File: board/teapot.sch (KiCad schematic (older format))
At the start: 42 parts, among them P1 BATT, P2 SMA, Q1 TEPT4400, U1 TPS79333DBVR, U2 TLV61225, U3 microusb-b, U4 RFM69W, U5 STM32L052K8, U6 HTU21D, U7 MS5637, U8 SWD, Y1 32.768k

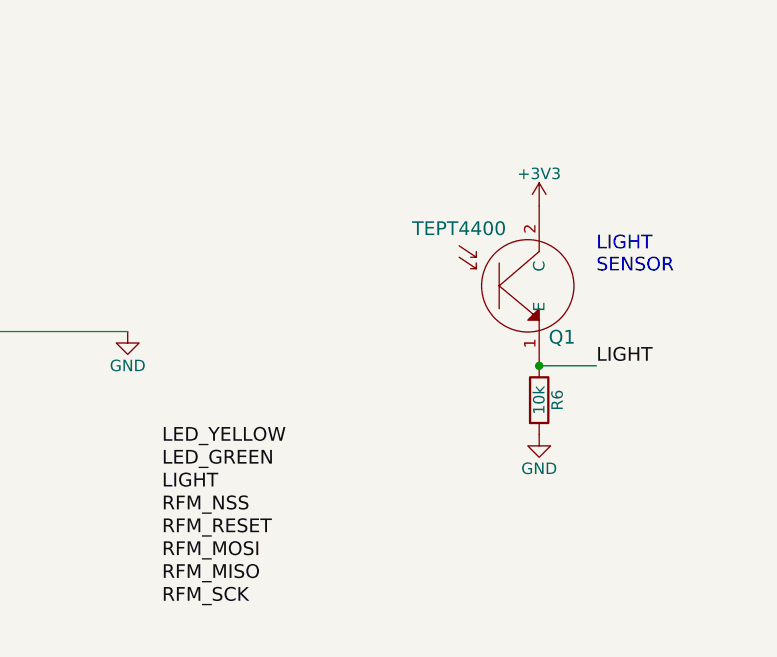
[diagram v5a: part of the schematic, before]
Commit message: Power consumption calculations
Resolves #5, resolves #2
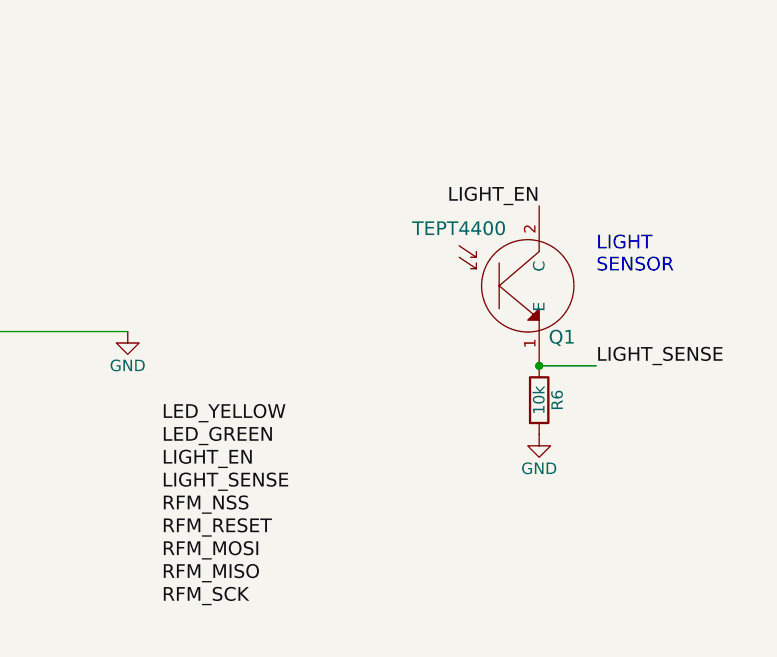
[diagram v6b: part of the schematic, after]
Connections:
- net +3V3: no longer Q1.2 (C)
- net LIGHT renamed LIGHT_SENSE
- new net LIGHT_EN: Q1.2 (C)
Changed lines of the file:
@@
-$EndComp
-$Comp
-L +3V3 #PWR013
-U 1 1 56709B94
-P 10200 3300
-F 0 "#PWR013" H 10200 3150 50  0001 C CNN
-F 1 "+3V3" H 10200 3440 50  0000 C CNN
-F 2 "" H 10200 3300 50  0000 C CNN
-F 3 "" H 10200 3300 50  0000 C CNN
-	1    10200 3300
-	1    0    0    -1
 $EndComp
 $Comp
@@
 I2C_SCK
 Text Label 10450 4000 0    60   ~ 0
-LIGHT
+LIGHT_SENSE
 Text Label 8750 1000 2    60   ~ 0
 RFM_RESET
@@
 I2C_SDA
 Text Label 8550 4550 0    60   ~ 0
-LIGHT
+LIGHT_SENSE
 Text Label 8550 4750 0    60   ~ 0
 RFM_RESET
@@
 	1    0    0    -1
 $EndComp
+Text Label 8550 4250 0    60   ~ 0
+LED_YELLOW
 Text Label 8550 4350 0    60   ~ 0
-LED_YELLOW
-Text Label 8550 4450 0    60   ~ 0
 LED_GREEN
 Text Label 1400 2850 2    60   ~ 0
@@
 	10650 1800 10800 1800
 Connection ~ 10800 1800
+Text Label 8550 4450 0    60   ~ 0
+LIGHT_EN
+Text Label 10200 3300 2    60   ~ 0
+LIGHT_EN
 $EndSCHEMATC

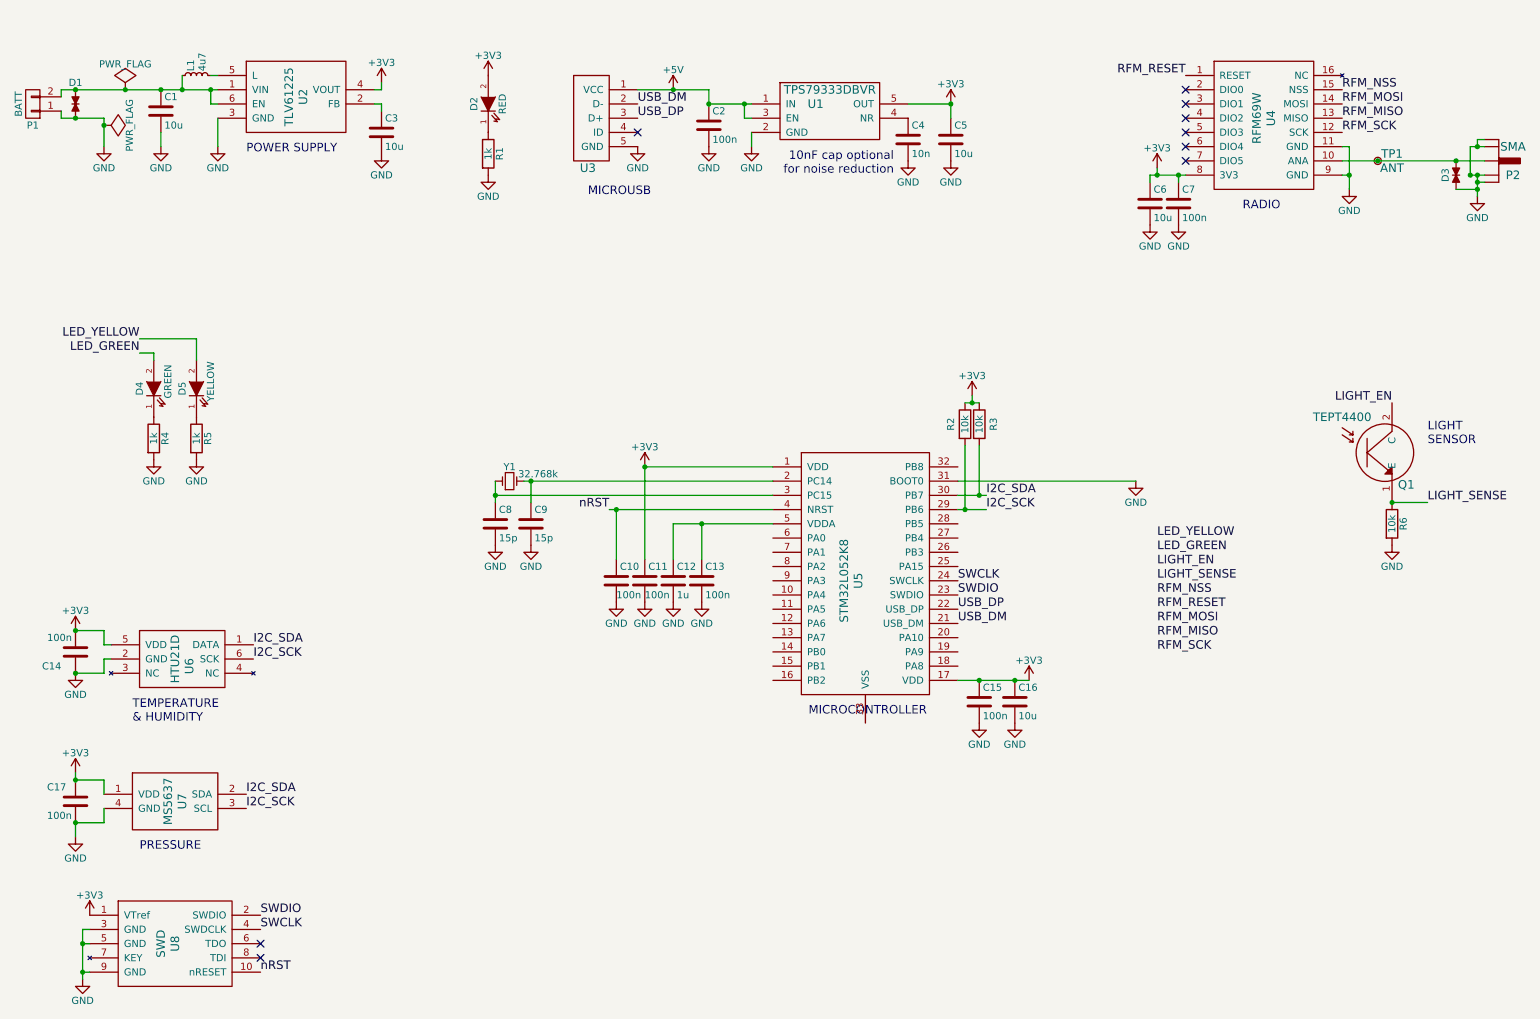
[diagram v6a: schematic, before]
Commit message: Added battery level monitor
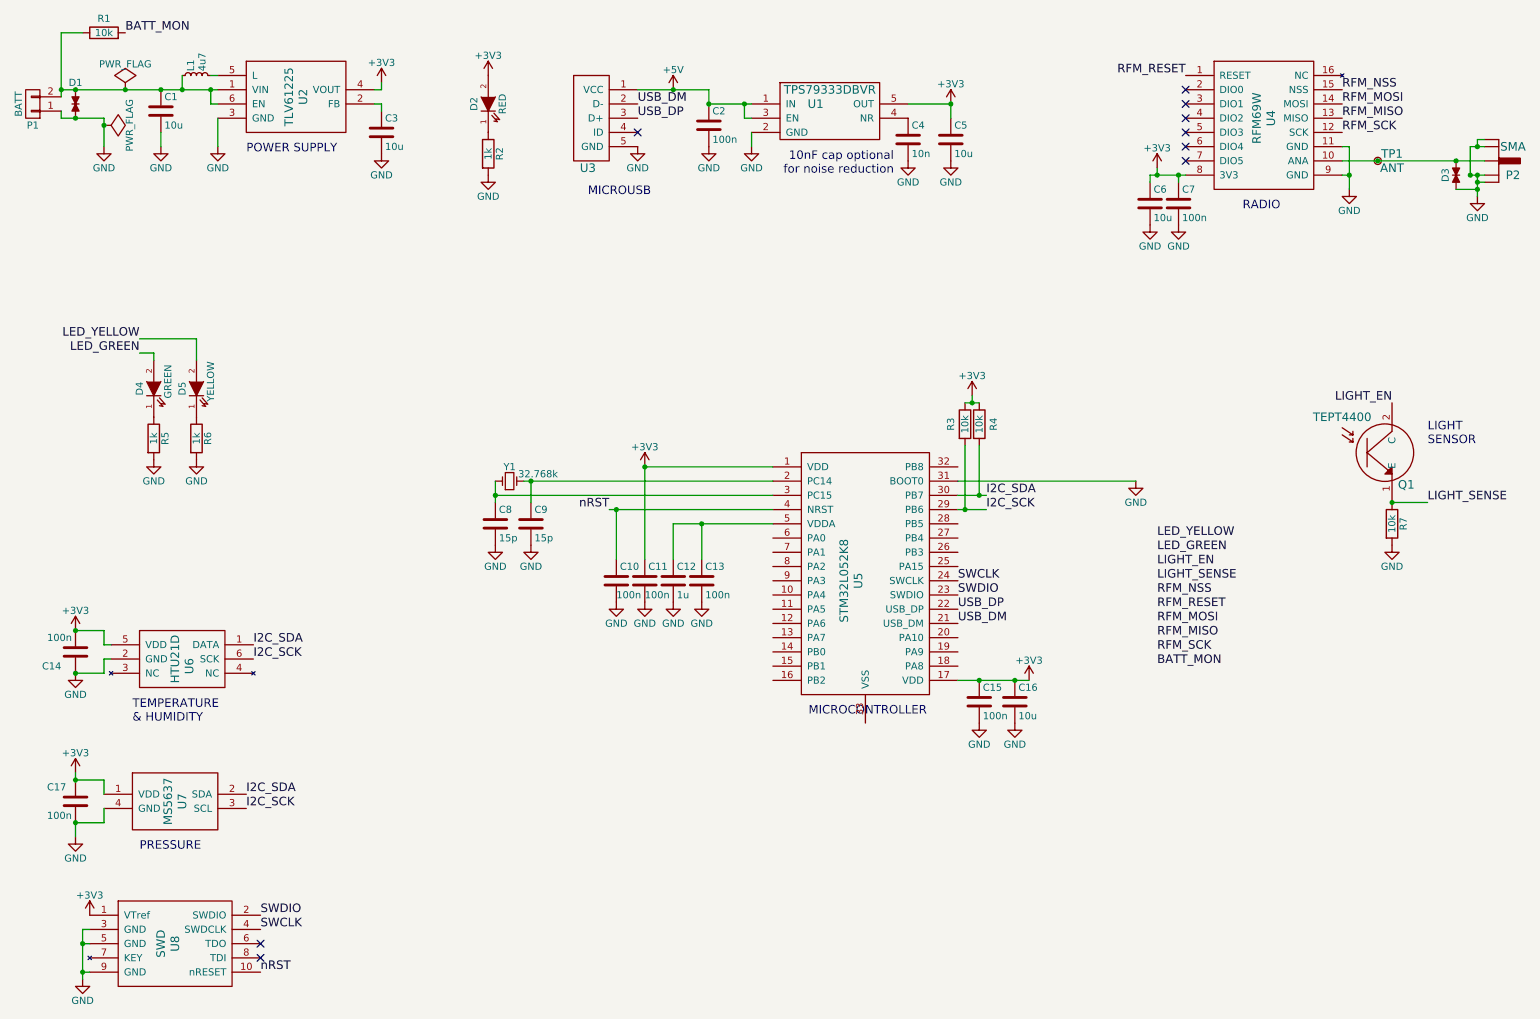
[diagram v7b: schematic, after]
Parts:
- added R1: 10k, Resistors_SMD:R_0805, symbol R
- renumbered R1 to R2, R2 to R3, R3 to R4, R4 to R5, R5 to R6, R6 to R7
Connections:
- net at C1.1, D1.1, L1.1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: now also R1.1
- new net BATT_MON: R1.2
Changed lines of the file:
@@
 $EndComp
 $Comp
-L R R3
+L R R4
 U 1 1 56708874
 P 7300 3450
-F 0 "R3" V 7400 3450 50  0000 C CNN
+F 0 "R4" V 7400 3450 50  0000 C CNN
 F 1 "10k" V 7300 3450 50  0000 C CNN
 F 2 "Resistors_SMD:R_0805" V 7230 3450 50  0001 C CNN
@@
 $EndComp
 $Comp
-L R R2
+L R R3
 U 1 1 567088B5
 P 7200 3450
-F 0 "R2" V 7100 3450 50  0000 C CNN
+F 0 "R3" V 7100 3450 50  0000 C CNN
 F 1 "10k" V 7200 3450 50  0000 C CNN
 F 2 "Resistors_SMD:R_0805" V 7130 3450 50  0001 C CNN
@@
 $EndComp
 $Comp
-L R R6
+L R R7
 U 1 1 56709F9B
 P 10200 4150
-F 0 "R6" V 10280 4150 50  0000 C CNN
+F 0 "R7" V 10280 4150 50  0000 C CNN
 F 1 "10k" V 10200 4150 50  0000 C CNN
 F 2 "Resistors_SMD:R_0805" V 10130 4150 50  0001 C CNN
@@
 $EndComp
 $Comp
-L GND #PWR014
+L GND #PWR013
 U 1 1 5670A6D2
 P 10200 4300
-F 0 "#PWR014" H 10200 4050 50  0001 C CNN
+F 0 "#PWR013" H 10200 4050 50  0001 C CNN
 F 1 "GND" H 10200 4150 50  0000 C CNN
 F 2 "" H 10200 4300 50  0000 C CNN
@@
 $EndComp
 $Comp
-L GND #PWR015
+L GND #PWR014
 U 1 1 5670C5C3
 P 10800 1850
-F 0 "#PWR015" H 10800 1600 50  0001 C CNN
+F 0 "#PWR014" H 10800 1600 50  0001 C CNN
 F 1 "GND" H 10800 1700 50  0000 C CNN
 F 2 "" H 10800 1850 50  0000 C CNN
@@
 $EndComp
 $Comp
-L GND #PWR016
+L GND #PWR015
 U 1 1 5670C6EB
 P 9900 1800
-F 0 "#PWR016" H 9900 1550 50  0001 C CNN
+F 0 "#PWR015" H 9900 1550 50  0001 C CNN
 F 1 "GND" H 9900 1650 50  0000 C CNN
 F 2 "" H 9900 1800 50  0000 C CNN
@@
 NoConn ~ 8750 1600
 $Comp
-L +3V3 #PWR017
+L +3V3 #PWR016
 U 1 1 5670C81E
 P 8550 1650
-F 0 "#PWR017" H 8550 1500 50  0001 C CNN
+F 0 "#PWR016" H 8550 1500 50  0001 C CNN
 F 1 "+3V3" H 8550 1790 50  0000 C CNN
 F 2 "" H 8550 1650 50  0000 C CNN
@@
 Connection ~ 8700 1700
 $Comp
-L GND #PWR018
+L GND #PWR017
 U 1 1 5670CC45
 P 8500 2050
-F 0 "#PWR018" H 8500 1800 50  0001 C CNN
+F 0 "#PWR017" H 8500 1800 50  0001 C CNN
 F 1 "GND" H 8500 1900 50  0000 C CNN
 F 2 "" H 8500 2050 50  0000 C CNN
@@
 $EndComp
 $Comp
-L GND #PWR019
+L GND #PWR018
 U 1 1 5670CC7F
 P 8700 2050
-F 0 "#PWR019" H 8700 1800 50  0001 C CNN
+F 0 "#PWR018" H 8700 1800 50  0001 C CNN
 F 1 "GND" H 8700 1900 50  0000 C CNN
 F 2 "" H 8700 2050 50  0000 C CNN
@@
 $EndComp
 $Comp
-L +3V3 #PWR020
+L +3V3 #PWR019
 U 1 1 5670D516
 P 3850 1000
-F 0 "#PWR020" H 3850 850 50  0001 C CNN
+F 0 "#PWR019" H 3850 850 50  0001 C CNN
 F 1 "+3V3" H 3850 1140 50  0000 C CNN
 F 2 "" H 3850 1000 50  0000 C CNN
@@
 $EndComp
 $Comp
-L R R1
+L R R2
 U 1 1 5670D552
 P 3850 1550
-F 0 "R1" V 3930 1550 50  0000 C CNN
+F 0 "R2" V 3930 1550 50  0000 C CNN
 F 1 "1k" V 3850 1550 50  0000 C CNN
 F 2 "Resistors_SMD:R_0805" V 3780 1550 50  0001 C CNN
@@
 $EndComp
 $Comp
-L GND #PWR021
+L GND #PWR020
 U 1 1 5670D5A3
 P 3850 1700
-F 0 "#PWR021" H 3850 1450 50  0001 C CNN
+F 0 "#PWR020" H 3850 1450 50  0001 C CNN
 F 1 "GND" H 3850 1550 50  0000 C CNN
 F 2 "" H 3850 1700 50  0000 C CNN
@@
 	1800 2850 1800 3000
 $Comp
-L R R4
+L R R5
 U 1 1 5670DB19
 P 1500 3550
-F 0 "R4" V 1580 3550 50  0000 C CNN
+F 0 "R5" V 1580 3550 50  0000 C CNN
 F 1 "1k" V 1500 3550 50  0000 C CNN
 F 2 "Resistors_SMD:R_0805" V 1430 3550 50  0001 C CNN
@@
 $EndComp
 $Comp
-L R R5
+L R R6
 U 1 1 5670DB64
 P 1800 3550
-F 0 "R5" V 1880 3550 50  0000 C CNN
+F 0 "R6" V 1880 3550 50  0000 C CNN
 F 1 "1k" V 1800 3550 50  0000 C CNN
 F 2 "Resistors_SMD:R_0805" V 1730 3550 50  0001 C CNN
@@
 $EndComp
 $Comp
-L GND #PWR022
+L GND #PWR021
 U 1 1 5670DC6D
 P 1500 3700
-F 0 "#PWR022" H 1500 3450 50  0001 C CNN
+F 0 "#PWR021" H 1500 3450 50  0001 C CNN
 F 1 "GND" H 1500 3550 50  0000 C CNN
 F 2 "" H 1500 3700 50  0000 C CNN
@@
 $EndComp
 $Comp
-L GND #PWR023
+L GND #PWR022
 U 1 1 5670DCB3
 P 1800 3700
-F 0 "#PWR023" H 1800 3450 50  0001 C CNN
+F 0 "#PWR022" H 1800 3450 50  0001 C CNN
 F 1 "GND" H 1800 3550 50  0000 C CNN
 F 2 "" H 1800 3700 50  0000 C CNN
@@
 nRST
 $Comp
-L +3V3 #PWR024
+L +3V3 #PWR023
 U 1 1 5670E977
 P 1050 6900
-F 0 "#PWR024" H 1050 6750 50  0001 C CNN
+F 0 "#PWR023" H 1050 6750 50  0001 C CNN
 F 1 "+3V3" H 1050 7040 50  0000 C CNN
 F 2 "" H 1050 6900 50  0000 C CNN
@@
 $EndComp
 $Comp
-L GND #PWR025
+L GND #PWR024
 U 1 1 5670E9BF
 P 1000 7350
-F 0 "#PWR025" H 1000 7100 50  0001 C CNN
+F 0 "#PWR024" H 1000 7100 50  0001 C CNN
 F 1 "GND" H 1000 7200 50  0000 C CNN
 F 2 "" H 1000 7350 50  0000 C CNN
@@
 $EndComp
 $Comp
-L GND #PWR026
+L GND #PWR025
 U 1 1 5675FB40
 P 4750 4700
-F 0 "#PWR026" H 4750 4450 50  0001 C CNN
+F 0 "#PWR025" H 4750 4450 50  0001 C CNN
 F 1 "GND" H 4750 4550 50  0000 C CNN
 F 2 "" H 4750 4700 50  0000 C CNN
@@
 $EndComp
 $Comp
-L GND #PWR027
+L GND #PWR026
 U 1 1 5675FC31
 P 8400 3850
-F 0 "#PWR027" H 8400 3600 50  0001 C CNN
+F 0 "#PWR026" H 8400 3600 50  0001 C CNN
 F 1 "GND" H 8400 3700 50  0000 C CNN
 F 2 "" H 8400 3850 50  0000 C CNN
@@
 	4750 4700 4750 4700
 $Comp
-L GND #PWR028
+L GND #PWR027
 U 1 1 56760E0A
 P 4950 4700
-F 0 "#PWR028" H 4950 4450 50  0001 C CNN
+F 0 "#PWR027" H 4950 4450 50  0001 C CNN
 F 1 "GND" H 4950 4550 50  0000 C CNN
 F 2 "" H 4950 4700 50  0000 C CNN
@@
 	4950 3750 4950 4400
 $Comp
-L +3V3 #PWR029
+L +3V3 #PWR028
 U 1 1 56760EFE
 P 4950 3750
-F 0 "#PWR029" H 4950 3600 50  0001 C CNN
+F 0 "#PWR028" H 4950 3600 50  0001 C CNN
 F 1 "+3V3" H 4950 3890 50  0000 C CNN
 F 2 "" H 4950 3750 50  0000 C CNN
@@
 Connection ~ 4950 3750
 $Comp
-L +3V3 #PWR030
+L +3V3 #PWR029
 U 1 1 5676102C
 P 7650 5250
-F 0 "#PWR030" H 7650 5100 50  0001 C CNN
+F 0 "#PWR029" H 7650 5100 50  0001 C CNN
 F 1 "+3V3" H 7650 5390 50  0000 C CNN
 F 2 "" H 7650 5250 50  0000 C CNN
@@
 Connection ~ 7300 5250
 $Comp
-L GND #PWR031
+L GND #PWR030
 U 1 1 5676123E
 P 7300 5550
-F 0 "#PWR031" H 7300 5300 50  0001 C CNN
+F 0 "#PWR030" H 7300 5300 50  0001 C CNN
 F 1 "GND" H 7300 5400 50  0000 C CNN
 F 2 "" H 7300 5550 50  0000 C CNN
@@
 $EndComp
 $Comp
-L GND #PWR032
+L GND #PWR031
 U 1 1 5676128E
 P 7550 5550
-F 0 "#PWR032" H 7550 5300 50  0001 C CNN
+F 0 "#PWR031" H 7550 5300 50  0001 C CNN
 F 1 "GND" H 7550 5400 50  0000 C CNN
 F 2 "" H 7550 5550 50  0000 C CNN
@@
 Connection ~ 5350 4150
 $Comp
-L GND #PWR033
+L GND #PWR032
 U 1 1 56761CAD
 P 5150 4700
-F 0 "#PWR033" H 5150 4450 50  0001 C CNN
+F 0 "#PWR032" H 5150 4450 50  0001 C CNN
 F 1 "GND" H 5150 4550 50  0000 C CNN
 F 2 "" H 5150 4700 50  0000 C CNN
@@
 $EndComp
 $Comp
-L GND #PWR034
+L GND #PWR033
 U 1 1 56761D01
 P 5350 4700
-F 0 "#PWR034" H 5350 4450 50  0001 C CNN
+F 0 "#PWR033" H 5350 4450 50  0001 C CNN
 F 1 "GND" H 5350 4550 50  0000 C CNN
 F 2 "" H 5350 4700 50  0000 C CNN
@@
 $EndComp
 $Comp
-L GND #PWR035
+L GND #PWR034
 U 1 1 56762871
 P 3900 4300
-F 0 "#PWR035" H 3900 4050 50  0001 C CNN
+F 0 "#PWR034" H 3900 4050 50  0001 C CNN
 F 1 "GND" H 3900 4150 50  0000 C CNN
 F 2 "" H 3900 4300 50  0000 C CNN
@@
 Connection ~ 4150 3850
 $Comp
-L GND #PWR036
+L GND #PWR035
 U 1 1 56762B31
 P 4150 4300
-F 0 "#PWR036" H 4150 4050 50  0001 C CNN
+F 0 "#PWR035" H 4150 4050 50  0001 C CNN
 F 1 "GND" H 4150 4150 50  0000 C CNN
 F 2 "" H 4150 4300 50  0000 C CNN
@@
 $EndComp
 $Comp
-L +5V #PWR037
+L +5V #PWR036
 U 1 1 567642B8
 P 5150 1100
-F 0 "#PWR037" H 5150 950 50  0001 C CNN
+F 0 "#PWR036" H 5150 950 50  0001 C CNN
 F 1 "+5V" H 5150 1240 50  0000 C CNN
 F 2 "" H 5150 1100 50  0000 C CNN
@@
 $EndComp
 $Comp
-L GND #PWR038
+L GND #PWR037
 U 1 1 56764314
 P 4900 1500
-F 0 "#PWR038" H 4900 1250 50  0001 C CNN
+F 0 "#PWR037" H 4900 1250 50  0001 C CNN
 F 1 "GND" H 4900 1350 50  0000 C CNN
 F 2 "" H 4900 1500 50  0000 C CNN
@@
 Connection ~ 5400 1200
 $Comp
-L GND #PWR039
+L GND #PWR038
 U 1 1 567852EE
 P 5400 1500
-F 0 "#PWR039" H 5400 1250 50  0001 C CNN
+F 0 "#PWR038" H 5400 1250 50  0001 C CNN
 F 1 "GND" H 5400 1350 50  0000 C CNN
 F 2 "" H 5400 1500 50  0000 C CNN
@@
 $EndComp
 $Comp
-L GND #PWR040
+L GND #PWR039
 U 1 1 5678534E
 P 5700 1500
-F 0 "#PWR040" H 5700 1250 50  0001 C CNN
+F 0 "#PWR039" H 5700 1250 50  0001 C CNN
 F 1 "GND" H 5700 1350 50  0000 C CNN
 F 2 "" H 5700 1500 50  0000 C CNN
@@
 	7100 1200 7100 1300
 $Comp
-L +3V3 #PWR041
+L +3V3 #PWR040
 U 1 1 56785888
 P 7100 1200
-F 0 "#PWR041" H 7100 1050 50  0001 C CNN
+F 0 "#PWR040" H 7100 1050 50  0001 C CNN
 F 1 "+3V3" H 7100 1340 50  0000 C CNN
 F 2 "" H 7100 1200 50  0000 C CNN
@@
 Connection ~ 7100 1200
 $Comp
-L GND #PWR042
+L GND #PWR041
 U 1 1 567858EE
 P 7100 1600
-F 0 "#PWR042" H 7100 1350 50  0001 C CNN
+F 0 "#PWR041" H 7100 1350 50  0001 C CNN
 F 1 "GND" H 7100 1450 50  0000 C CNN
 F 2 "" H 7100 1600 50  0000 C CNN
@@
 $EndComp
 $Comp
-L GND #PWR043
+L GND #PWR042
 U 1 1 56785952
 P 6800 1600
-F 0 "#PWR043" H 6800 1350 50  0001 C CNN
+F 0 "#PWR042" H 6800 1350 50  0001 C CNN
 F 1 "GND" H 6800 1450 50  0000 C CNN
 F 2 "" H 6800 1600 50  0000 C CNN
@@
 $EndComp
 Wire Wire Line
-	850  1150 850  1100
+	850  700  850  1150
 Wire Wire Line
 	850  1250 850  1300
@@
 Text Label 10200 3300 2    60   ~ 0
 LIGHT_EN
+Wire Wire Line
+	850  700  1000 700
+Connection ~ 850  1100
+$Comp
+L R R1
+U 1 1 5678C9FB
+P 1150 700
+F 0 "R1" V 1250 700 50  0000 C CNN
+F 1 "10k" V 1150 700 50  0000 C CNN
+F 2 "Resistors_SMD:R_0805" V 1080 700 50  0001 C CNN
+F 3 "" H 1150 700 50  0000 C CNN
+F 4 "2502786" H 1150 700 60  0001 C CNN "Farnell"
+	1    1150 700
+	0    -1   -1   0
+$EndComp
+Text Label 1300 700  0    60   ~ 0
+BATT_MON
+Text Label 8550 5150 0    60   ~ 0
+BATT_MON
 $EndSCHEMATC
